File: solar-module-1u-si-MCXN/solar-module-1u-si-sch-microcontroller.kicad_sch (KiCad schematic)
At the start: 42 parts, among them J2 Conn_01x02, J3 OreSat Debug, U1 MCXN947VKLT, U11 TCAN330, U2 TMP101NA/3KSLOTTED, U7 TMP101NA/3KSLOTTED, Y2 24 MHz

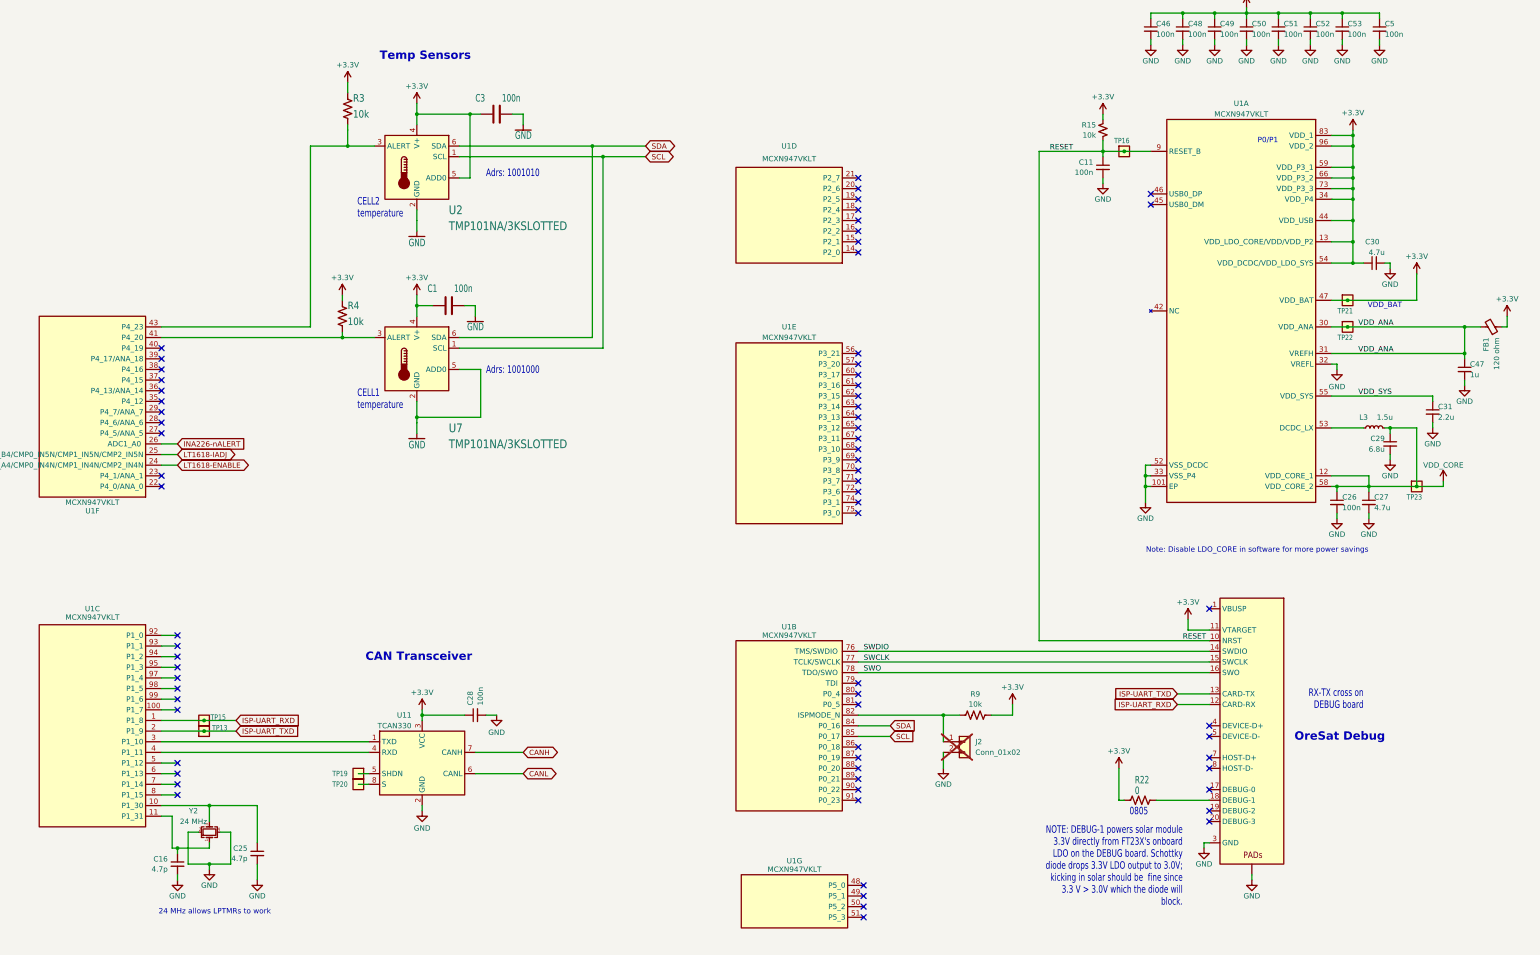
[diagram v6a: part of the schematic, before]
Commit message: Final polishing before fab. Fixed I2C pullups, removed some silly test points, lots of good zone planning on layer 3, cleaned up solar ideal diodes, moved LED to a blink light instead of power light.
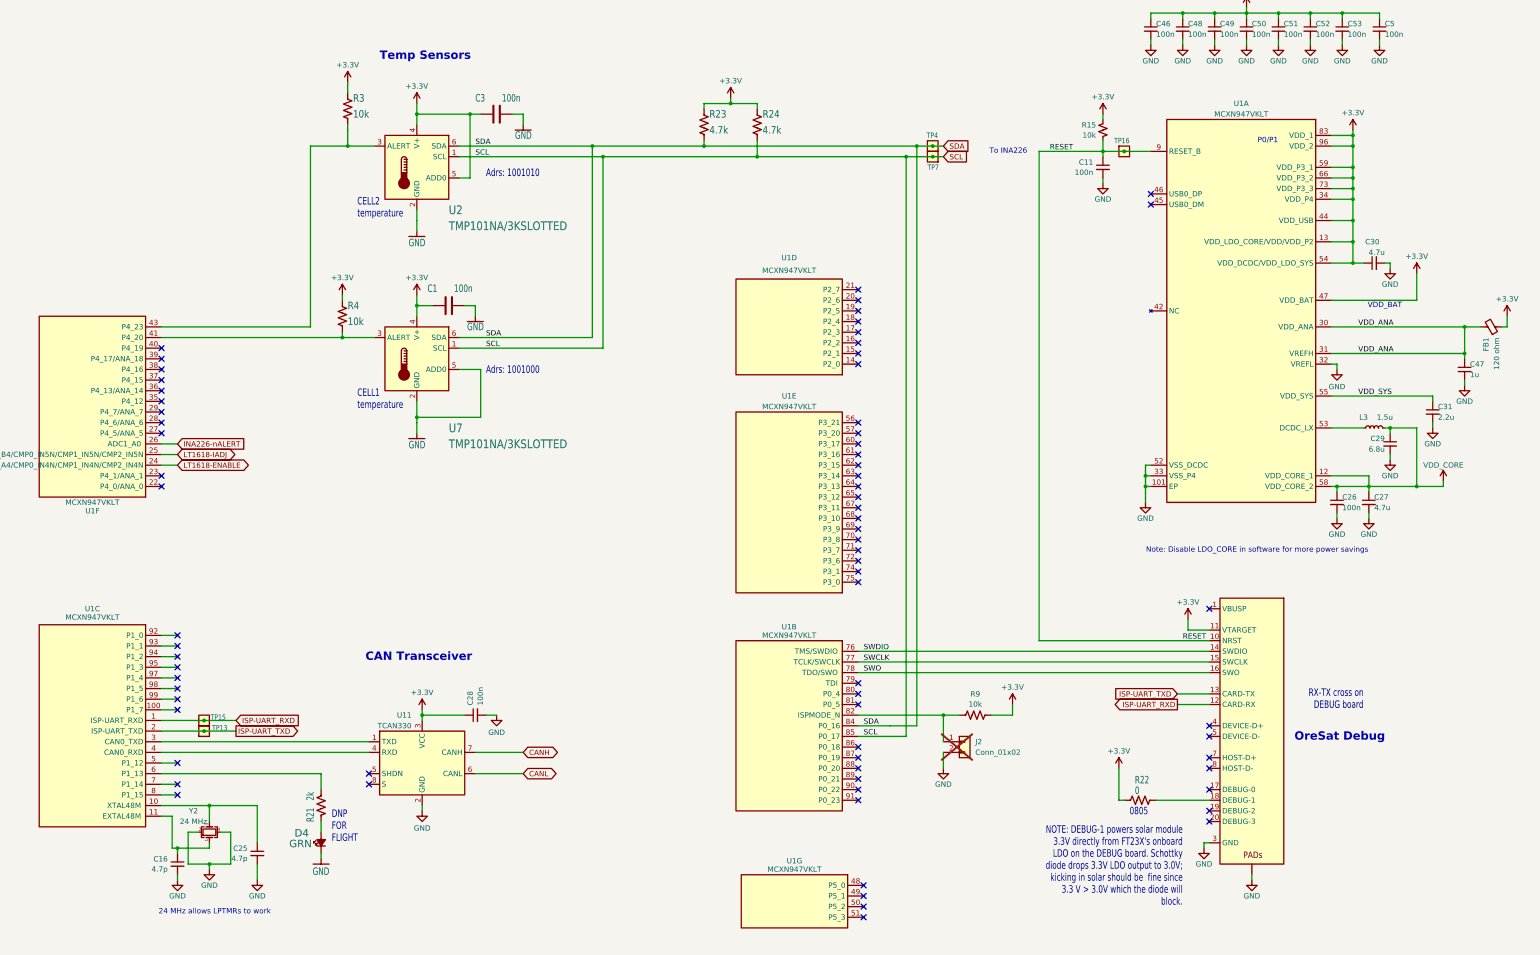
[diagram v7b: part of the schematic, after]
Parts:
- removed TP19, TP20, TP21, TP22, TP23: Test-Point, oresat-misc:TestPoint-0.75mm-th, symbol oresat-misc:Test-Point-0.75mm-th
- added D4: GRN, LED_SMD:LED_0603_1608Metric, symbol Device:LED_Small_Filled
- added R21: 2k, oresat-passives:0603-C-NOSILK, symbol Device:R_US
- added R23, R24: 4.7k, oresat-passives:0603-C-NOSILK, symbol Device:R_US
- added TP4, TP7: Test-Point, oresat-misc:TestPoint-0.75mm-th, symbol oresat-misc:Test-Point-0.75mm-th
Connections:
- net +3.3V: now also R23.2, R24.2
- net GND: now also D4.1 (K)
- net SCL: now also R24.1, TP7.1
- net SDA: now also R23.1, TP4.1
- net at U1.6 (P1_13): now also R21.1
- new net: D4.2 (A), R21.2
- no-connect marks 70 -> 71
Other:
- note added: "DNP FOR FLIGHT"
- note added: "To INA226"
- title: OreSat Solar Module - Silicon Cells -> OreSat Solar Module - Silicon Cells + MCXN
- moved on the sheet: U1D, U1E

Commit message: Fix up BOM
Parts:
- C1, C3, R3, R4: DIS Digi-Key -> DigiKey
- C11, C26, C28, C46, C48, C49, C5, C50, C51, C52, C53: DIS (none) -> DigiKey; DPN (none) -> 587-3472-1-ND; MFR Murata Electronics -> Taiyo Yuden; MPN GRM188R72A104KA35D -> TMK107BJ104KAHT
- C16, C25: DIS (none) -> DigiKey; DPN (none) -> 490-GRM1885C1H4R7WA01DCT-ND; MFR Murata Electronics -> Murata
- C27, C30: DIS (none) -> DigiKey; DPN (none) -> 587-4332-1-ND; MFR Murata Electronics -> Taiyo Yuden; MPN GRM188R61E475KE11D -> EMK107BBJ475KAHT
- C29: DIS (none) -> DigiKey; DPN (none) -> 445-12661-1-ND; MFR Murata Electronics -> TDK Corporation; MPN GCJ31CR71A685KA13L -> CGA4J1X5R1C685K125AC
- C31: DIS (none) -> DigiKey; DPN (none) -> 587-4929-1-ND; MFR Murata Electronics -> Taiyo Yuden; MPN GRM188R61E225KA12D -> TMK107BBJ225MAHT
- C47: DIS (none) -> DigiKey; DPN (none) -> 587-3473-1-ND; MFR Murata Electronics -> Taiyo Yuden; MPN GRM185R61E105KA12J -> TMK107BJ105KAHT
- D4: value GRN -> AMBER; DIS Digi-Key -> DigiKey; DPN 732-4971-1-ND -> 732-150060AS75000CT-ND; MPN 150060GS75000 -> 150060AS75000
- FB1: DIS (none) -> DIgiKey; DPN (none) -> 1934-1472-1-ND
- J3: DIS (none) -> DIgiKey; DPN (none) -> A100287CT-ND
- L3: DIS (none) -> DIgiKey; DPN (none) -> 118-SRP2012TMA-1R5MCT-ND
- R15: DIS (none) -> DigiKey; DPN (none) -> RMCF0603FT10K0CT-ND
- R23, R24: DIS Digi-Key -> DIgiKey; DPN RMCF0603FT10K0CT-ND -> RMCF0603FT4K70CT-ND; MPN RMCF0603FT10K0 -> RMCF0603FT4K70
- R9: DIS (none) -> DigiKey; DPN (none) -> RMCF0603FT10K0CT-ND; MFR (none) -> Stackpole Electronics Inc; MPN (none) -> RMCF0603FT10K0
- U1: DIS (none) -> Mouser; DPN (none) -> 771-MCXN947VKLT
- U11: DIS (none) -> DigiKey; DPN (none) -> 296-46215-1-ND
- U2, U7: DIS Digi-Key -> DIgiKey
- Y2: DIS (none) -> DIgiKey; DPN (none) -> 1923-830108212309CT-ND
